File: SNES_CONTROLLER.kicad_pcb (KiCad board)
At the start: 2 copper layers, 57 x 76 mm, 24 parts, among them J2 Screw_Terminal_01x12, J3 Screw_Terminal_01x12, J4 Screw_Terminal_01x05, U1 4021, U2 4021

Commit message: Add labels to front silkscreen and mount holes
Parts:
- added H1: MountingHole, MountingHole:MountingHole_3.2mm_M3, F.Cu at (106.5, 66.0)
- added H2: MountingHole, MountingHole:MountingHole_3.2mm_M3, F.Cu at (146.5, 66.0)
- added H3: MountingHole, MountingHole:MountingHole_3.2mm_M3, F.Cu at (126.5, 129.0)
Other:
- board text added: "SEL"
- board text added: "SNES & Uzebox controller PCB v1.1"
- board text removed: "SELECT"
- board text removed: "SNES & Uzebox controller PCB v1.0"

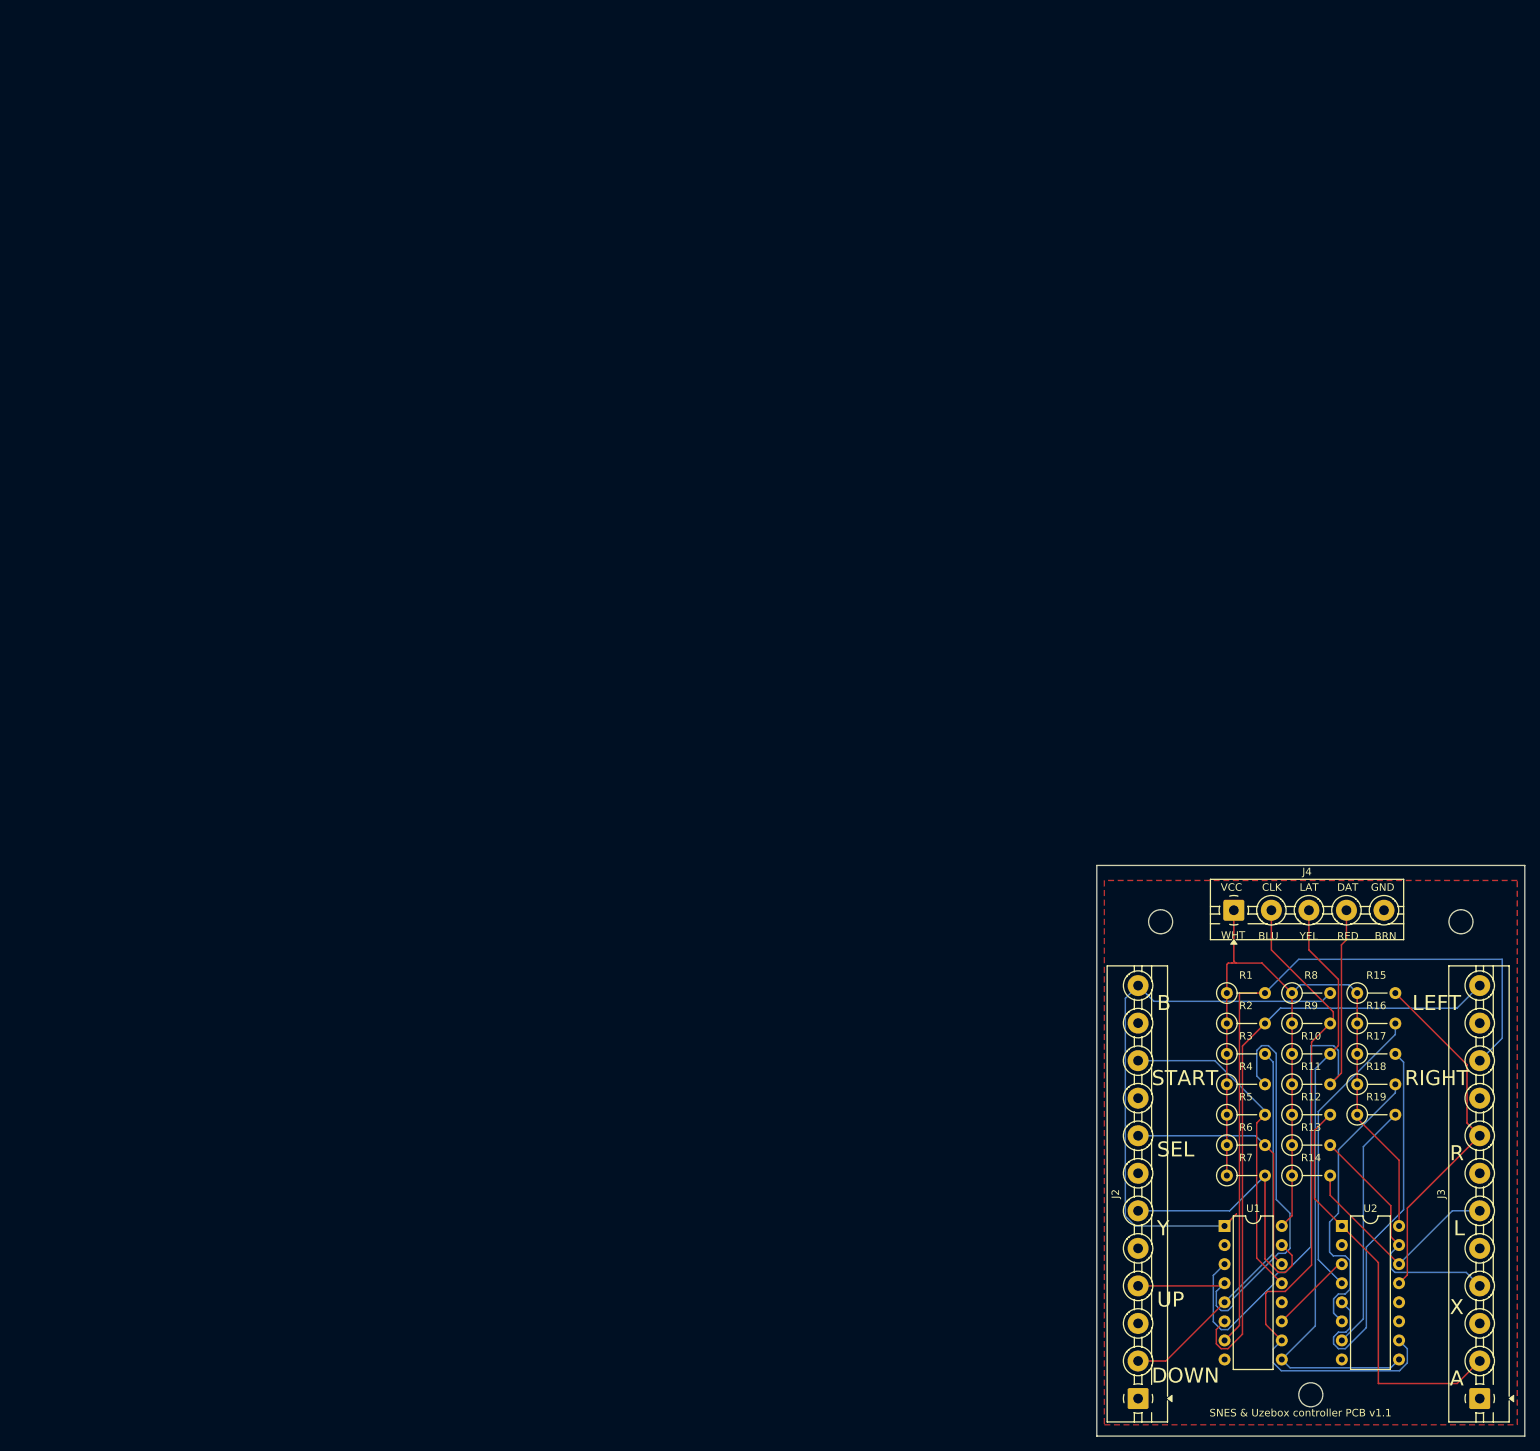
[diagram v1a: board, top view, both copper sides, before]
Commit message: v1.2 - Use M4 mount holes
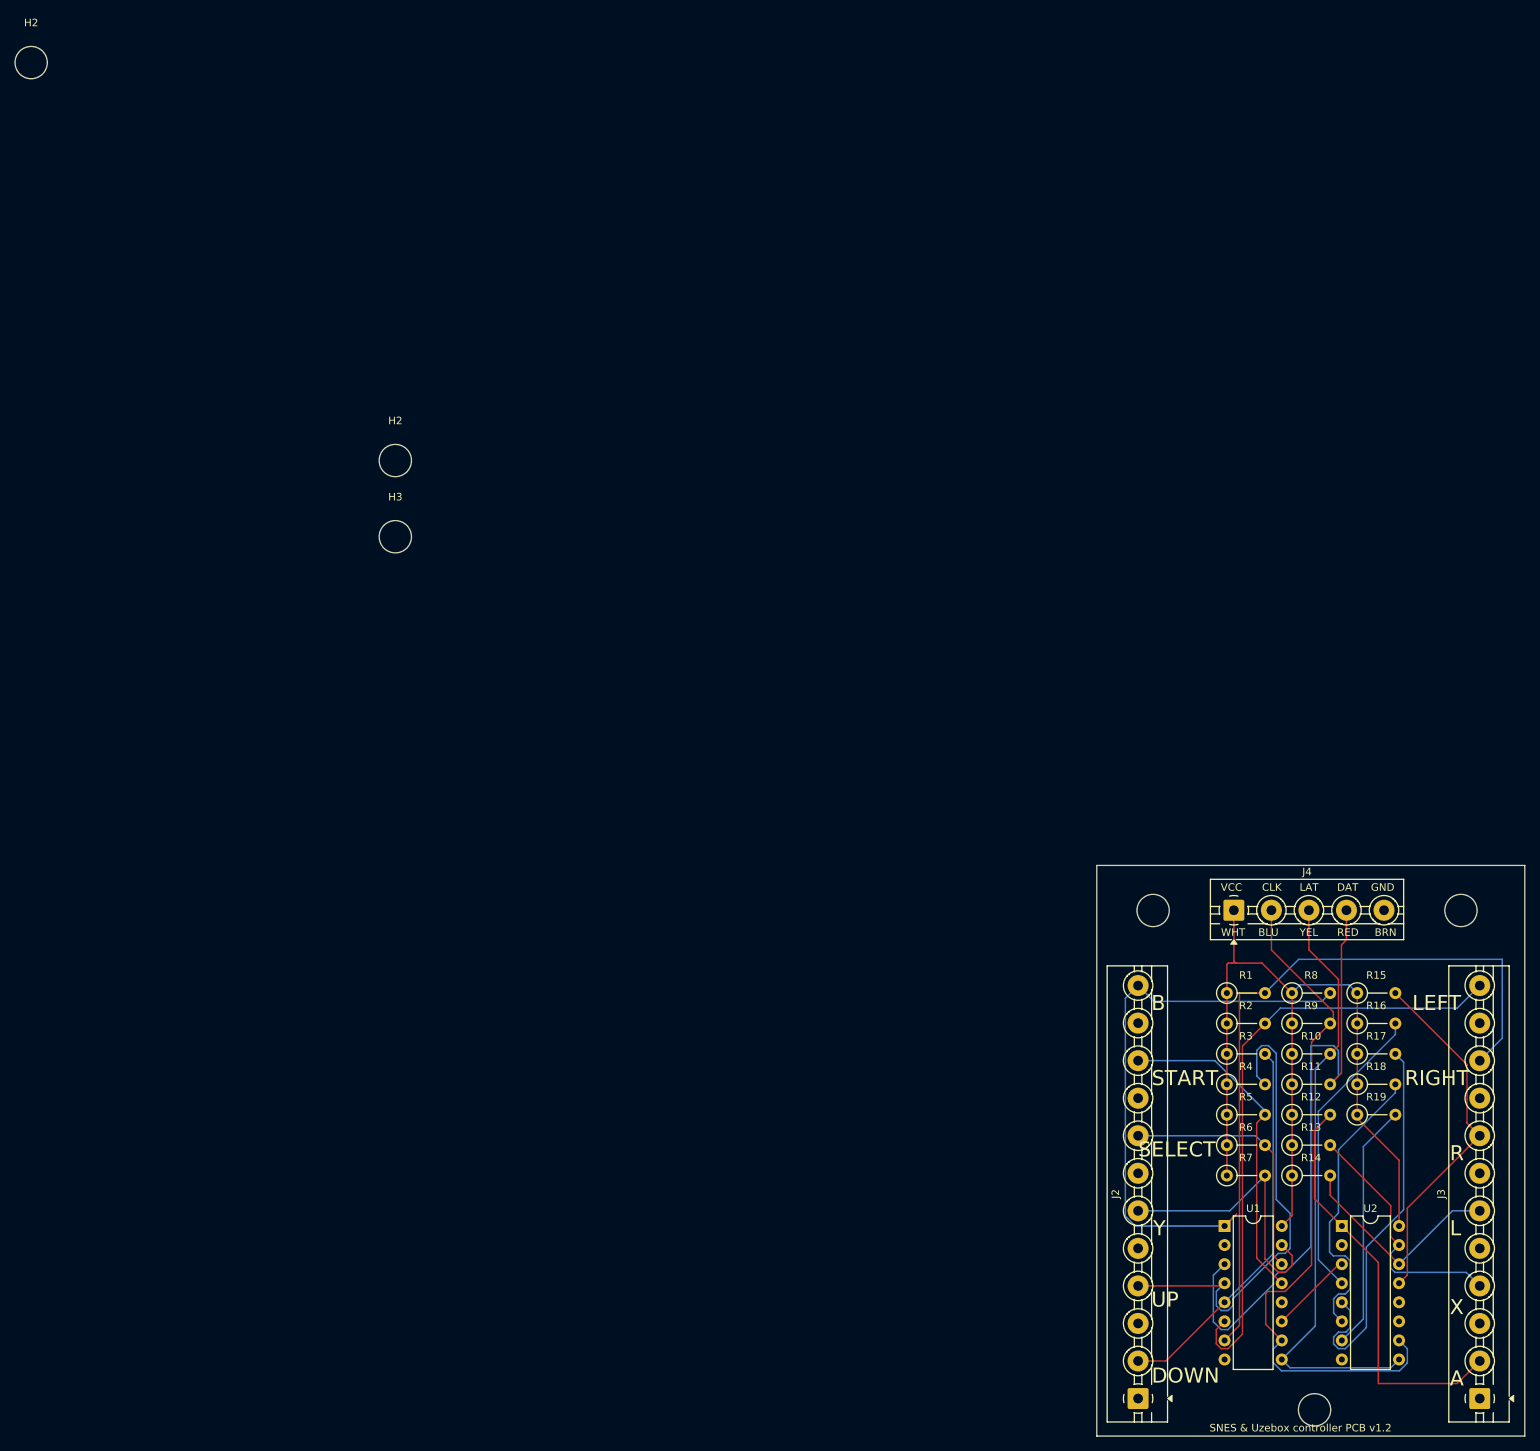
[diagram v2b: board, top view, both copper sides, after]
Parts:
- removed the H2 at (146.5, 66.0)
- added H2: MountingHole, MountingHole:MountingHole_4.3mm_M4, F.Cu at (-43.9, -48.4)
- added H2: MountingHole, MountingHole:MountingHole_4.3mm_M4, F.Cu at (4.58, 4.58)
- added REF**: MountingHole_4.3mm_M4, MountingHole:MountingHole_4.3mm_M4, F.Cu at (105.5, 64.5)
- added REF**: MountingHole_4.3mm_M4, MountingHole:MountingHole_4.3mm_M4, F.Cu at (146.5, 64.5)
- H1, H3: footprint MountingHole:MountingHole_3.2mm_M3 -> MountingHole:MountingHole_4.3mm_M4
- moved H3 167.1 mm to (4.58, 14.7)
- moved H1 68.2 mm to (127.0, 131.0)
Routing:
- removed copper zone on F.Cu, net /Gnd
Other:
- board text added: "SELECT"
- board text added: "SNES & Uzebox controller PCB v1.2"
- board text removed: "SEL"
- board text removed: "SNES & Uzebox controller PCB v1.1"

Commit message: Move mount holes and top silkscreen labels - v1.3
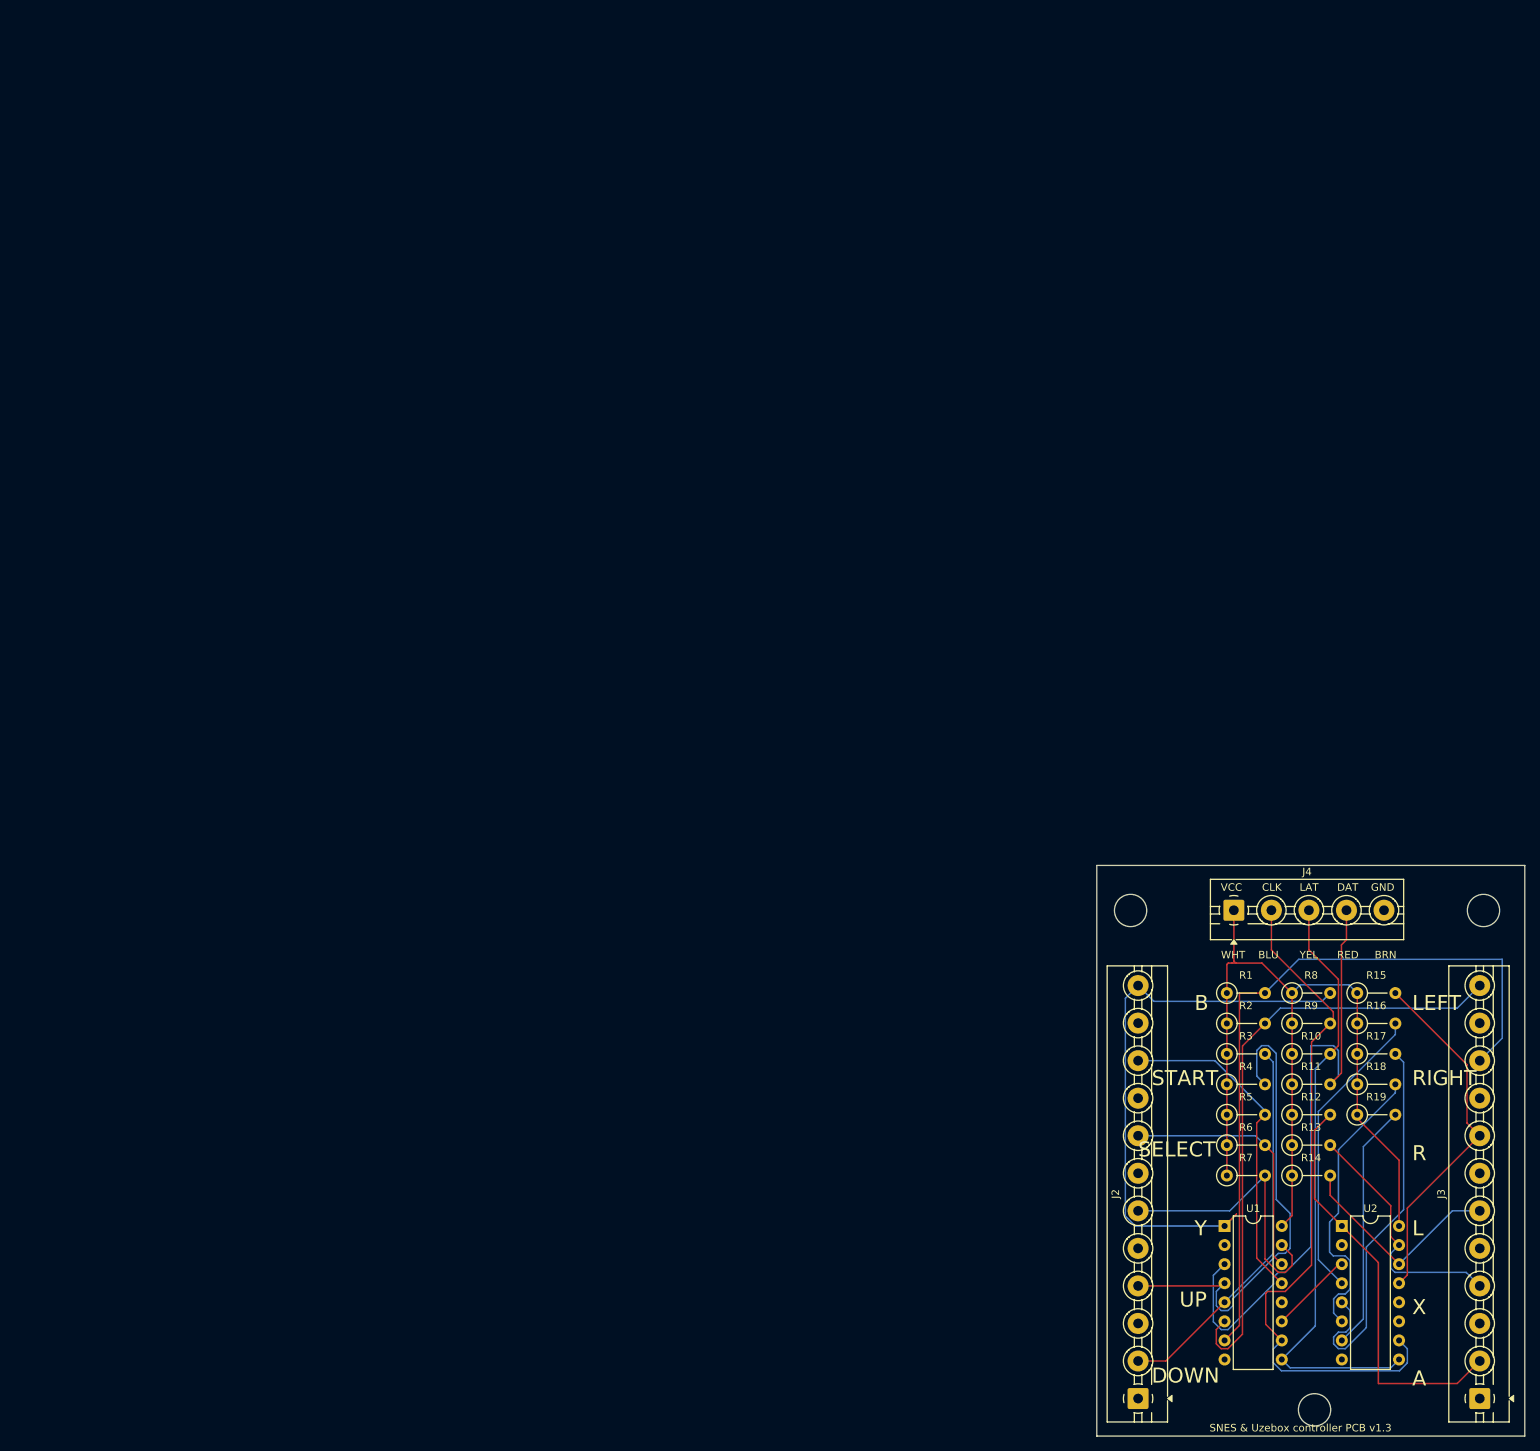
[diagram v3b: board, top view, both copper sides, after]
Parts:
- removed H2 (x2), H3: MountingHole, MountingHole:MountingHole_4.3mm_M4
- moved REF** 3.00 mm to (102.5, 64.5)
- moved REF** 3.00 mm to (149.5, 64.5)
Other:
- board text added: "SNES & Uzebox controller PCB v1.3"
- board text removed: "SNES & Uzebox controller PCB v1.2"
